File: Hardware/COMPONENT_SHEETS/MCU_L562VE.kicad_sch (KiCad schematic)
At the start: 33 parts, among them SW1 MCU Reset, U7 STM32L562VET6Q, Y3 32MHz

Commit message: Fixed incorrect LCSC numbers
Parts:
- R11: LCSC C23253 -> C25999
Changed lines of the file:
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@@
       (effects (font (size 1.27 1.27)) hide)
     )
-    (property "LCSC" " C23253 " (id 4) (at 242.57 78.105 0)
+    (property "LCSC" "C25999" (id 4) (at 242.57 78.105 0)
       (effects (font (size 1.27 1.27)) hide)
     )

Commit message: Initial import of STM32L562ZET6
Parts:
- removed U7: STM32L562VET6Q, Package_QFP:LQFP-100_14x14mm_P0.5mm, symbol RDT_Custom_Symbols:STM32L562VET
- added IC1: STM32L562ZET6, QFP50P2200X2200X160-144N, symbol STM32L562ZET6:STM32L562ZET6
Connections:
- net DEBUG_SWCLK: now also IC1.109 (PA14)
- net DEBUG_SWDIO: now also IC1.105 (PA13)
- net I2C1_EN: now also IC1.136 (PB6)
- net NRST: now also IC1.25 (NRST)
- net SPI1_MISO: now also IC1.42 (PA6)
- net SPI1_MOSI: now also IC1.43 (PA7)
- net SPI1_SCK: now also IC1.41 (PA5)
- net SPI2_EXT_INT: now also IC1.78 (PD9)
- net SPI2_RST: now also IC1.77 (PD8)
- net SPI3_EXT_INT: now also IC1.115 (PD1)
- net SPI3_MISO: now also IC1.112 (PC11)
- net SPI3_MOSI: now also IC1.113 (PC12)
- net SPI3_RST: now also IC1.110 (PA15)
- net SPI3_SCK: now also IC1.111 (PC10)
- net USB_D+: now also IC1.104 (PA12)
- net USB_D-: now also IC1.103 (PA11)
- net ~{SPI1_NSS}: now also IC1.46 (PB0)
- net ~{SPI2_NSS}: now also IC1.114 (PD0)
- net ~{SPI3_NSS}: now also IC1.40 (PA4)
- net at C24.1, Y3.1: now also IC1.23 (PH0-OSC_IN)
- net at C25.1, Y3.2: now also IC1.24 (PH1-OSC_OUT)
- net at D6.2 (A): now also IC1.58 (PE7)
- net at D5.2 (A): now also IC1.59 (PE8)
- net at D4.2 (A): now also IC1.60 (PE9)
- net at D3.2 (A): now also IC1.63 (PE10)
- net at D2.2 (A): now also IC1.64 (PE11)
- net at JP1.2 (C), R12.2: now also IC1.138 (PH3-BOOT0)
- no-connect marks 46 -> 28
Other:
- moved on the sheet: C24, C25, C33, C37, C38, D2, D3, D4, D5, D6, JP1, R10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

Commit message: Schematic complete with STM32L562ZET6
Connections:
- net +3V3: now also C33.2, IC1.106 (VDDUSB), IC1.108 (VDD_7), IC1.121 (VDD_8), IC1.131 (VDDIO2_2), IC1.144 (VDD_9), IC1.17 (VDD_1), IC1.32 (VREF+), IC1.33 (VDDA), IC1.38 (VSS_2), IC1.52 (VDD_3), IC1.6 (VBAT), IC1.72 (VDD_5), IC1.84 (VDD_6), IC1.95 (VDDIO2_1); no longer C33.1
- net ABORT_1: now also IC1.69 (PB10)
- net ABORT_2: now also IC1.70 (PB11)
- net GND: now also C33.1, IC1.107 (VSS_8), IC1.120 (VSS_9), IC1.130 (VSS_10), IC1.143 (VSS_11), IC1.16 (VSS_1), IC1.30 (VSSA), IC1.31 (VREF-), IC1.39 (VDD_2), IC1.51 (VSS_3), IC1.71 (VSS_5), IC1.83 (VSS_6), IC1.94 (VSS_7); no longer C33.2
- net I2C1_SCL: now also IC1.139 (PB8)
- net I2C1_SDA: now also IC1.140 (PB9)
- net SPI2_MISO: now also IC1.75 (PB14)
- net SPI2_MOSI: now also IC1.76 (PB15)
- net SPI2_SCK: now also IC1.74 (PB13)
- no-connect marks 28 -> 82
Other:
- moved on the sheet: C24, C25, C33, C37, C38, D2, D3, D4, D5, D6, R10, R6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

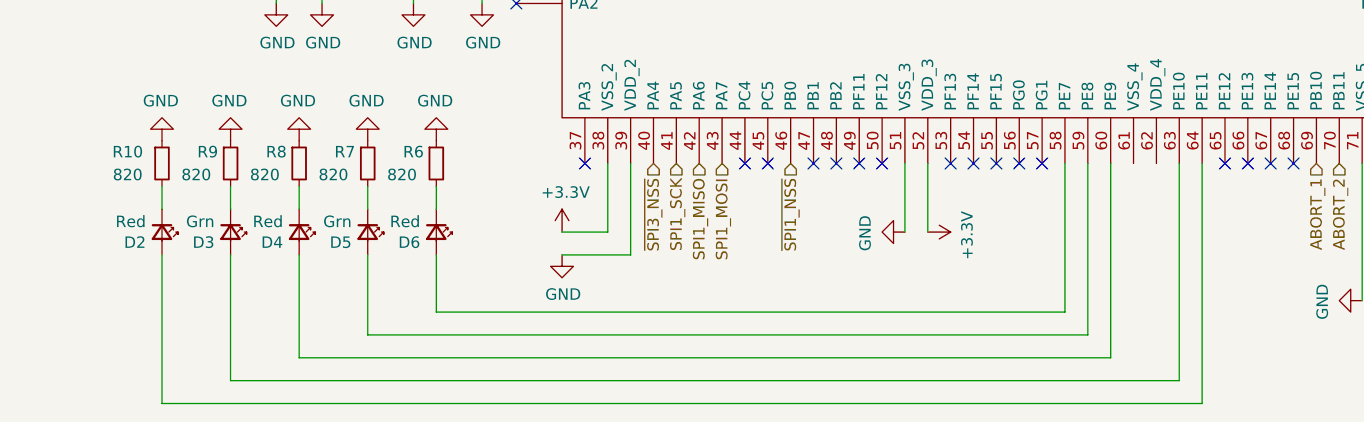
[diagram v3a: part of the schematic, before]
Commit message: started changing chip on-board
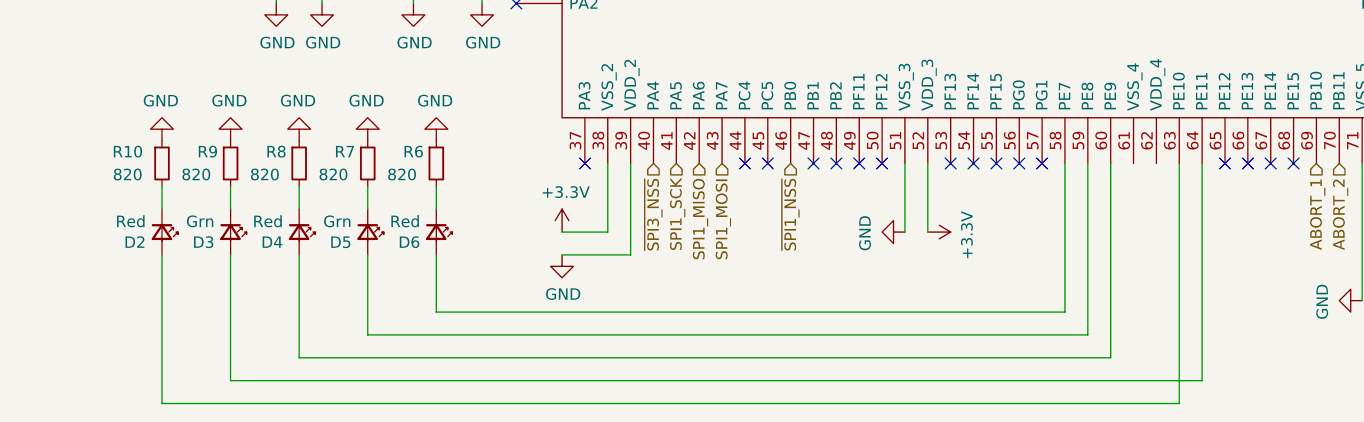
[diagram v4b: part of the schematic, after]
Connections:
- net at D2.2 (A): now also IC1.63 (PE10); no longer IC1.64 (PE11)
- net at D3.2 (A): now also IC1.64 (PE11); no longer IC1.63 (PE10)
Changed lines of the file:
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@@
   (no_connect (at 110.49 40.64))
   (no_connect (at 74.93 114.3))
-  (wire (pts (xy 148.59 170.18) (xy 148.59 194.31))
-    (stroke (width 0) (type default) (color 0 0 0 0))
-  )
   (wire (pts (xy 194.31 63.5) (xy 179.07 63.5))
     (stroke (width 0) (type default) (color 0 0 0 0))
@@
     (stroke (width 0) (type default) (color 0 0 0 0))
   )
-  (wire (pts (xy 148.59 194.31) (xy 43.18 194.31))
+  (wire (pts (xy 43.18 194.31) (xy 151.13 194.31))
     (stroke (width 0) (type default) (color 0 0 0 0))
   )
@@
     (stroke (width 0) (type default) (color 0 0 0 0))
   )
+  (wire (pts (xy 151.13 170.18) (xy 151.13 194.31))
+    (stroke (width 0) (type default) (color 0 0 0 0))
+  )
   (wire (pts (xy 53.34 142.24) (xy 63.5 142.24))
     (stroke (width 0) (type default) (color 0 0 0 0))
@@
     (stroke (width 0) (type default) (color 0 0 0 0))
   )
-  (wire (pts (xy 151.13 196.85) (xy 35.56 196.85))
+  (wire (pts (xy 35.56 196.85) (xy 148.59 196.85))
     (stroke (width 0) (type default) (color 0 0 0 0))
   )
@@
     (stroke (width 0) (type default) (color 0 0 0 0))
   )
+  (wire (pts (xy 148.59 170.18) (xy 148.59 196.85))
+    (stroke (width 0) (type default) (color 0 0 0 0))
+  )
   (wire (pts (xy 181.61 41.91) (xy 191.77 41.91))
     (stroke (width 0) (type default) (color 0 0 0 0))
@@
   )
   (wire (pts (xy 203.2 34.29) (xy 203.2 35.56))
-    (stroke (width 0) (type default) (color 0 0 0 0))
-  )
-  (wire (pts (xy 151.13 170.18) (xy 151.13 196.85))
     (stroke (width 0) (type default) (color 0 0 0 0))
   )
@@
   (symbol (lib_id "power:+3.3V") (at 82.55 34.29 90) (unit 1)
     (in_bom yes) (on_board yes)
-    (property "Reference" "#PWR?" (id 0) (at 86.36 34.29 0)
+    (property "Reference" "#PWR0112" (id 0) (at 86.36 34.29 0)
       (effects (font (size 1.27 1.27)) hide)
     )
@@
   (symbol (lib_id "power:GND") (at 184.15 127 0) (unit 1)
     (in_bom yes) (on_board yes)
-    (property "Reference" "#PWR?" (id 0) (at 184.15 133.35 0)
+    (property "Reference" "#PWR0119" (id 0) (at 184.15 133.35 0)
       (effects (font (size 1.27 1.27)) hide)
     )
@@
   (symbol (lib_id "power:+3.3V") (at 194.31 63.5 0) (unit 1)
     (in_bom yes) (on_board yes)
-    (property "Reference" "#PWR?" (id 0) (at 194.31 67.31 0)
+    (property "Reference" "#PWR0124" (id 0) (at 194.31 67.31 0)
       (effects (font (size 1.27 1.27)) hide)
     )
@@
   (symbol (lib_id "power:GND") (at 71.12 152.4 0) (unit 1)
     (in_bom yes) (on_board yes)
-    (property "Reference" "#PWR?" (id 0) (at 71.12 158.75 0)
+    (property "Reference" "#PWR0111" (id 0) (at 71.12 158.75 0)
       (effects (font (size 1.27 1.27)) hide)
     )
@@
   (symbol (lib_id "power:+3.3V") (at 120.65 177.8 270) (unit 1)
     (in_bom yes) (on_board yes)
-    (property "Reference" "#PWR?" (id 0) (at 116.84 177.8 0)
+    (property "Reference" "#PWR0116" (id 0) (at 116.84 177.8 0)
       (effects (font (size 1.27 1.27)) hide)
     )
@@
   (symbol (lib_id "power:+3.3V") (at 140.97 33.02 90) (unit 1)
     (in_bom yes) (on_board yes)
-    (property "Reference" "#PWR?" (id 0) (at 144.78 33.02 0)
+    (property "Reference" "#PWR0120" (id 0) (at 144.78 33.02 0)
       (effects (font (size 1.27 1.27)) hide)
     )
@@
   (symbol (lib_id "power:GND") (at 198.12 68.58 0) (unit 1)
     (in_bom yes) (on_board yes)
-    (property "Reference" "#PWR?" (id 0) (at 198.12 74.93 0)
+    (property "Reference" "#PWR0125" (id 0) (at 198.12 74.93 0)
       (effects (font (size 1.27 1.27)) hide)
     )
@@
   (symbol (lib_id "power:GND") (at 143.51 33.02 90) (unit 1)
     (in_bom yes) (on_board yes)
-    (property "Reference" "#PWR?" (id 0) (at 149.86 33.02 0)
+    (property "Reference" "#PWR0121" (id 0) (at 149.86 33.02 0)
       (effects (font (size 1.27 1.27)) hide)
     )
@@
   (symbol (lib_id "power:GND") (at 184.15 99.06 0) (unit 1)
     (in_bom yes) (on_board yes)
-    (property "Reference" "#PWR?" (id 0) (at 184.15 105.41 0)
+    (property "Reference" "#PWR0128" (id 0) (at 184.15 105.41 0)
       (effects (font (size 1.27 1.27)) hide)
     )
@@
   (symbol (lib_id "power:+3.3V") (at 69.85 63.5 0) (unit 1)
     (in_bom yes) (on_board yes)
-    (property "Reference" "#PWR?" (id 0) (at 69.85 67.31 0)
+    (property "Reference" "#PWR0114" (id 0) (at 69.85 67.31 0)
       (effects (font (size 1.27 1.27)) hide)
     )
@@
   (symbol (lib_id "power:+3.3V") (at 184.15 96.52 0) (unit 1)
     (in_bom yes) (on_board yes)
-    (property "Reference" "#PWR?" (id 0) (at 184.15 100.33 0)
+    (property "Reference" "#PWR0127" (id 0) (at 184.15 100.33 0)
       (effects (font (size 1.27 1.27)) hide)
     )
@@
   (symbol (lib_id "power:GND") (at 118.11 33.02 90) (unit 1)
     (in_bom yes) (on_board yes)
-    (property "Reference" "#PWR?" (id 0) (at 124.46 33.02 0)
+    (property "Reference" "#PWR0123" (id 0) (at 124.46 33.02 0)
       (effects (font (size 1.27 1.27)) hide)
     )
@@
   (symbol (lib_id "power:+3.3V") (at 80.01 177.8 0) (unit 1)
     (in_bom yes) (on_board yes)
-    (property "Reference" "#PWR?" (id 0) (at 80.01 181.61 0)
+    (property "Reference" "#PWR0110" (id 0) (at 80.01 181.61 0)
       (effects (font (size 1.27 1.27)) hide)
     )
@@
   (symbol (lib_id "power:+3.3V") (at 115.57 33.02 90) (unit 1)
     (in_bom yes) (on_board yes)
-    (property "Reference" "#PWR?" (id 0) (at 119.38 33.02 0)
+    (property "Reference" "#PWR0122" (id 0) (at 119.38 33.02 0)
       (effects (font (size 1.27 1.27)) hide)
     )
@@
   (symbol (lib_id "power:GND") (at 80.01 180.34 0) (unit 1)
     (in_bom yes) (on_board yes)
-    (property "Reference" "#PWR?" (id 0) (at 80.01 186.69 0)
+    (property "Reference" "#PWR0109" (id 0) (at 80.01 186.69 0)
       (effects (font (size 1.27 1.27)) hide)
     )
@@
   (symbol (lib_id "power:GND") (at 168.91 185.42 270) (unit 1)
     (in_bom yes) (on_board yes)
-    (property "Reference" "#PWR?" (id 0) (at 162.56 185.42 0)
+    (property "Reference" "#PWR0117" (id 0) (at 162.56 185.42 0)
       (effects (font (size 1.27 1.27)) hide)
     )
@@
   (symbol (lib_id "power:+3.3V") (at 171.45 185.42 270) (unit 1)
     (in_bom yes) (on_board yes)
-    (property "Reference" "#PWR?" (id 0) (at 167.64 185.42 0)
+    (property "Reference" "#PWR0118" (id 0) (at 167.64 185.42 0)
       (effects (font (size 1.27 1.27)) hide)
     )
@@
   (symbol (lib_id "power:+3.3V") (at 184.15 124.46 0) (unit 1)
     (in_bom yes) (on_board yes)
-    (property "Reference" "#PWR?" (id 0) (at 184.15 128.27 0)
+    (property "Reference" "#PWR0126" (id 0) (at 184.15 128.27 0)
       (effects (font (size 1.27 1.27)) hide)
     )
@@
   (symbol (lib_id "power:GND") (at 118.11 177.8 270) (unit 1)
     (in_bom yes) (on_board yes)
-    (property "Reference" "#PWR?" (id 0) (at 111.76 177.8 0)
+    (property "Reference" "#PWR0115" (id 0) (at 111.76 177.8 0)
       (effects (font (size 1.27 1.27)) hide)
     )
@@
   (symbol (lib_id "power:GND") (at 85.09 34.29 90) (unit 1)
     (in_bom yes) (on_board yes)
-    (property "Reference" "#PWR?" (id 0) (at 91.44 34.29 0)
-      (effects (font (size 1.27 1.27)) hide)
-    )
+    (property "Reference" "#PWR0113" (id 0) (at 91.44 34.29 0)
+      (effects (font (size 1.27 1.27)) hide)
+    )

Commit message: Initial routing pass
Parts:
- IC1: LCSC (none) -> C1236660
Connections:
- net +3V3: now also IC1.62 (VDD_4)
- net GND: now also IC1.61 (VSS_4)
- net at D2.2 (A): now also IC1.64 (PE11); no longer IC1.63 (PE10)
- net at D3.2 (A): now also IC1.63 (PE10); no longer IC1.64 (PE11)
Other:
- moved on the sheet: C24, C25, C33, C37, C38, D2, D3, D4, D5, D6, IC1, JP1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
